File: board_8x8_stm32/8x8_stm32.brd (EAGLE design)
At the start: 100 x 100 mm, 96 parts, among them IC1 STM32F0, J1 SWD_SHROUD, Q1 BSS123, Q10 BSS84, Q11 BSS84, Q12 BSS84, Q13 BSS84, Q14 BSS84, Q15 BSS84, Q16 BSS84, Q2 BSS123, Q3 BSS123, Q4 BSS123, Q5 BSS123, Q6 BSS123, Q7 BSS123, Q8 BSS123, Q9 BSS84

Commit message: adding led photodide sim
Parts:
- removed D1, D2, D3, D4, D5, D6, D7, D8: (no value), dtb:SOD123
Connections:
- removed net CHARGE: D1.C, D2.C, D3.C, D4.C, D5.C, D6.C, D7.C, D8.C
- net ROW1: no longer D1.A
- net ROW2: no longer D2.A
- net ROW3: no longer D3.A
- net ROW4: no longer D4.A
- net ROW5: no longer D5.A
- net ROW6: no longer D6.A
- net ROW7: no longer D7.A
- net ROW8: no longer D8.A
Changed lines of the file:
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@@
 <element name="Q15" library="transistor-small-signal" package="SOT23" value="BSS84" x="67.29" y="41.4" rot="R270"/>
 <element name="Q16" library="transistor-small-signal" package="SOT23" value="BSS84" x="79.29" y="59.02" rot="R270"/>
-<element name="D1" library="dtb" package="SOD123" value="" x="-16.51" y="69.85"/>
-<element name="D2" library="dtb" package="SOD123" value="" x="-22.86" y="69.85"/>
-<element name="D3" library="dtb" package="SOD123" value="" x="-29.21" y="69.85"/>
-<element name="D4" library="dtb" package="SOD123" value="" x="-35.56" y="69.85"/>
-<element name="D5" library="dtb" package="SOD123" value="" x="-41.91" y="69.85"/>
-<element name="D6" library="dtb" package="SOD123" value="" x="-48.26" y="69.85"/>
-<element name="D7" library="dtb" package="SOD123" value="" x="-54.61" y="69.85"/>
-<element name="D8" library="dtb" package="SOD123" value="" x="-60.96" y="69.85"/>
 <element name="J1" library="dtb" package="SWD_PTH_SHROUD" value="SWD_SHROUD" x="75" y="49.9" rot="MR270"/>
 <element name="SV1" library="con-lstb" package="MA03-2" value="" x="50.27" y="74.08">
@@
 <contactref element="LED8" pad="A"/>
 <contactref element="Q9" pad="3"/>
-<contactref element="D1" pad="A"/>
-<wire x1="-14.61" y1="69.85" x2="36.44" y2="73.77" width="0" layer="19" extent="1-1"/>
-<wire x1="-44.45" y1="61.48" x2="-14.61" y2="69.85" width="0" layer="19" extent="1-1"/>
+<wire x1="-44.45" y1="61.48" x2="36.44" y2="73.77" width="0" layer="19" extent="1-1"/>
 </signal>
 <signal name="ROW2">
@@
 <contactref element="LED15" pad="A"/>
 <contactref element="Q10" pad="3"/>
-<contactref element="D2" pad="A"/>
-<wire x1="-20.96" y1="69.85" x2="26.82" y2="73.77" width="0" layer="19" extent="1-1"/>
-<wire x1="-52.07" y1="31" x2="-20.96" y2="69.85" width="0" layer="19" extent="1-1"/>
+<wire x1="-52.07" y1="31" x2="26.82" y2="73.77" width="0" layer="19" extent="1-1"/>
 <wire x1="-55.88" y1="31" x2="-52.07" y2="31" width="0" layer="19" extent="1-1"/>
 </signal>
@@
 <contactref element="LED24" pad="A"/>
 <contactref element="Q11" pad="3"/>
-<contactref element="D3" pad="A"/>
 <wire x1="67.77" y1="65.8" x2="93.75" y2="68" width="0" layer="19" extent="1-1"/>
-<wire x1="-27.31" y1="69.85" x2="67.77" y2="65.8" width="0" layer="19" extent="1-1"/>
 </signal>
 <signal name="ROW4">
 <contactref element="LED32" pad="A"/>
 <contactref element="Q16" pad="3"/>
-<contactref element="D4" pad="A"/>
 <wire x1="80.39" y1="59.02" x2="93.75" y2="55.5" width="0" layer="19" extent="1-1"/>
-<wire x1="-33.66" y1="69.85" x2="80.39" y2="59.02" width="0" layer="19" extent="1-1"/>
 </signal>
 <signal name="ROW5">
 <contactref element="LED40" pad="A"/>
 <contactref element="Q15" pad="3"/>
-<contactref element="D5" pad="A"/>
 <wire x1="68.39" y1="41.4" x2="93.75" y2="43" width="0" layer="19" extent="1-1"/>
-<wire x1="-40.01" y1="69.85" x2="68.39" y2="41.4" width="0" layer="19" extent="1-1"/>
 </signal>
 <signal name="ROW6">
 <contactref element="LED48" pad="A"/>
 <contactref element="Q14" pad="3"/>
-<contactref element="D6" pad="A"/>
 <wire x1="80.39" y1="28.78" x2="93.75" y2="30.5" width="0" layer="19" extent="1-1"/>
-<wire x1="-46.36" y1="69.85" x2="80.39" y2="28.78" width="0" layer="19" extent="1-1"/>
 </signal>
 <signal name="ROW7">
@@
 <contactref element="LED55" pad="A"/>
 <contactref element="Q13" pad="3"/>
-<contactref element="D7" pad="A"/>
 <wire x1="81.25" y1="18" x2="93.75" y2="18" width="0" layer="19" extent="1-1"/>
 <wire x1="68.75" y1="18" x2="81.25" y2="18" width="0" layer="19" extent="1-1"/>
@@
 <wire x1="18.75" y1="18" x2="31.25" y2="18" width="0" layer="19" extent="1-1"/>
 <wire x1="6.25" y1="18" x2="18.75" y2="18" width="0" layer="19" extent="1-1"/>
-<wire x1="-52.71" y1="69.85" x2="6.25" y2="18" width="0" layer="19" extent="1-1"/>
 </signal>
 <signal name="ROW8">
@@
 <contactref element="LED57" pad="A"/>
 <contactref element="Q12" pad="3"/>
-<contactref element="D8" pad="A"/>
 <wire x1="81.25" y1="5.5" x2="93.75" y2="5.5" width="0" layer="19" extent="1-1"/>
 <wire x1="68.75" y1="5.5" x2="81.25" y2="5.5" width="0" layer="19" extent="1-1"/>
@@
 <wire x1="18.75" y1="5.5" x2="31.25" y2="5.5" width="0" layer="19" extent="1-1"/>
 <wire x1="6.25" y1="5.5" x2="18.75" y2="5.5" width="0" layer="19" extent="1-1"/>
-<wire x1="-59.06" y1="69.85" x2="6.25" y2="5.5" width="0" layer="19" extent="1-1"/>
 </signal>
 <signal name="COL8">
@@
 <wire x1="29" y1="32.9" x2="40.48" y2="32.045" width="0" layer="19" extent="1-1"/>
 </signal>
-<signal name="CHARGE">
-<contactref element="D1" pad="C"/>
-<contactref element="D8" pad="C"/>
-<contactref element="D7" pad="C"/>
-<contactref element="D6" pad="C"/>
-<contactref element="D5" pad="C"/>
-<contactref element="D4" pad="C"/>
-<contactref element="D3" pad="C"/>
-<contactref element="D2" pad="C"/>
-<wire x1="-24.76" y1="69.85" x2="-18.41" y2="69.85" width="0" layer="19" extent="1-1"/>
-<wire x1="-31.11" y1="69.85" x2="-24.76" y2="69.85" width="0" layer="19" extent="1-1"/>
-<wire x1="-37.46" y1="69.85" x2="-31.11" y2="69.85" width="0" layer="19" extent="1-1"/>
-<wire x1="-43.81" y1="69.85" x2="-37.46" y2="69.85" width="0" layer="19" extent="1-1"/>
-<wire x1="-50.16" y1="69.85" x2="-43.81" y2="69.85" width="0" layer="19" extent="1-1"/>
-<wire x1="-56.51" y1="69.85" x2="-50.16" y2="69.85" width="0" layer="19" extent="1-1"/>
-<wire x1="-62.86" y1="69.85" x2="-56.51" y2="69.85" width="0" layer="19" extent="1-1"/>
-</signal>
 <signal name="RFET1">

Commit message: playing about with different deisgns
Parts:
- moved Q13 46.4 mm to (79.5, 16.4), turned to 0 degrees
- moved Q12 46.2 mm to (79.3, 3.92), turned to 0 degrees
- moved Q8 13.9 mm to (72.8, 31.0), turned to 180 degrees
- moved Q11 12.8 mm to (79.5, 66.2), turned to 0 degrees
- moved Q15 12.3 mm to (79.6, 41.0), turned to 0 degrees
- moved Q5 11.9 mm to (65.5, 31.0)
- moved J1 11.5 mm to (86.5, 49.6)
- moved Q16 5.25 mm to (79.7, 53.8), turned to 0 degrees
- moved RN2 4.46 mm to (69.2, 27.5), turned to 0 degrees
- moved Q6 3.25 mm to (59.2, 31.0)
- moved Q7 1.82 mm to (53.5, 30.8), turned to 180 degrees
- moved Q14 0.50 mm to (79.7, 29.0), turned to 0 degrees
- moved LED36 0.50 mm to (43.8, 43.8)
- moved IC1 0.26 mm to (50.0, 49.9), turned to 180 degrees
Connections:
- removed net SHIFT_CLK: SV2.2, SV4.2
- new net N$9: Q10.2, Q11.2, Q12.2, Q13.2, Q14.2, Q15.2, Q16.2, Q9.2
- new net SHIFT_LEFT: SV4.5
- new net SHIFT_RIGHT: SV2.5
- net CFET1: now also IC1.18
- net CFET2: now also IC1.19
- net CFET3: now also IC1.20
- net CFET4: now also IC1.39
- net CFET5: now also IC1.40
- net CFET6: now also IC1.41
- net CFET7: now also IC1.42
- net CFET8: now also IC1.43
- net COL1: now also IC1.45
- net COL2: now also IC1.46
- net COL3: now also IC1.21
- net COL4: now also IC1.22
- net COL5: now also IC1.25
- net COL6: now also IC1.26
- net COL7: now also IC1.27
- net COL8: now also IC1.28
- net ROW1: now also LED1.A, LED2.A, LED3.A, LED4.A, LED5.A, LED6.A, LED7.A
- net ROW2: now also LED10.A, LED11.A, LED12.A, LED13.A, LED14.A, LED9.A
- net ROW3: now also LED17.A, LED18.A, LED19.A, LED20.A, LED21.A, LED22.A, LED23.A
- net ROW4: now also LED25.A, LED26.A, LED27.A, LED28.A, LED29.A, LED30.A, LED31.A
- net ROW5: now also LED33.A, LED34.A, LED35.A, LED36.A, LED37.A, LED38.A, LED39.A
- net ROW6: now also LED41.A, LED42.A, LED43.A, LED44.A, LED45.A, LED46.A, LED47.A
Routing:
- net COL8: track 0.00 -> 149.2 mm, vias 0 -> 9
- net COL1: track 0.00 -> 132.3 mm, vias 0 -> 7
- net COL2: track 0.00 -> 118.4 mm, vias 0 -> 7
- net ROW5: track 0.00 -> 92.6 mm, vias 0 -> 5
- net ROW3: track 0.00 -> 88.2 mm
- net COL3: track 0.00 -> 88.0 mm, vias 0 -> 6
- net ROW4: track 0.00 -> 83.2 mm
- net COL7: track 0.00 -> 76.5 mm, vias 0 -> 7
- net SWDAT: track 0.00 -> 41.9 mm, vias 0 -> 4
- net COL6: track 0.00 -> 41.5 mm, vias 0 -> 4
- net GND: track 0.00 -> 39.4 mm, vias 0 -> 4
- net COL5: track 0.00 -> 36.0 mm, vias 0 -> 4
- net SWCLK: track 0.00 -> 35.0 mm, vias 0 -> 2
- net CFET8: track 0.00 -> 33.6 mm
- net CFET7: track 0.00 -> 28.8 mm, vias 0 -> 2
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
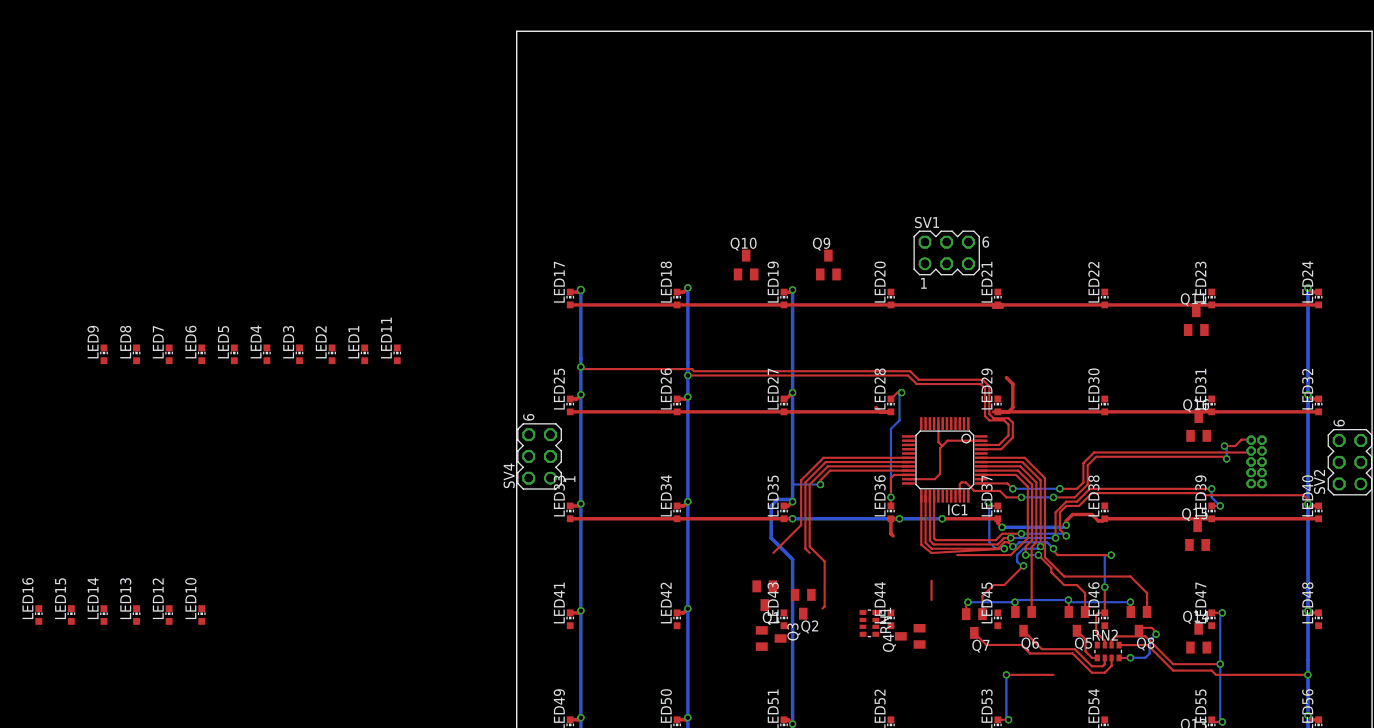
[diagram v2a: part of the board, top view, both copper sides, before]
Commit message: postioning components to the top edge
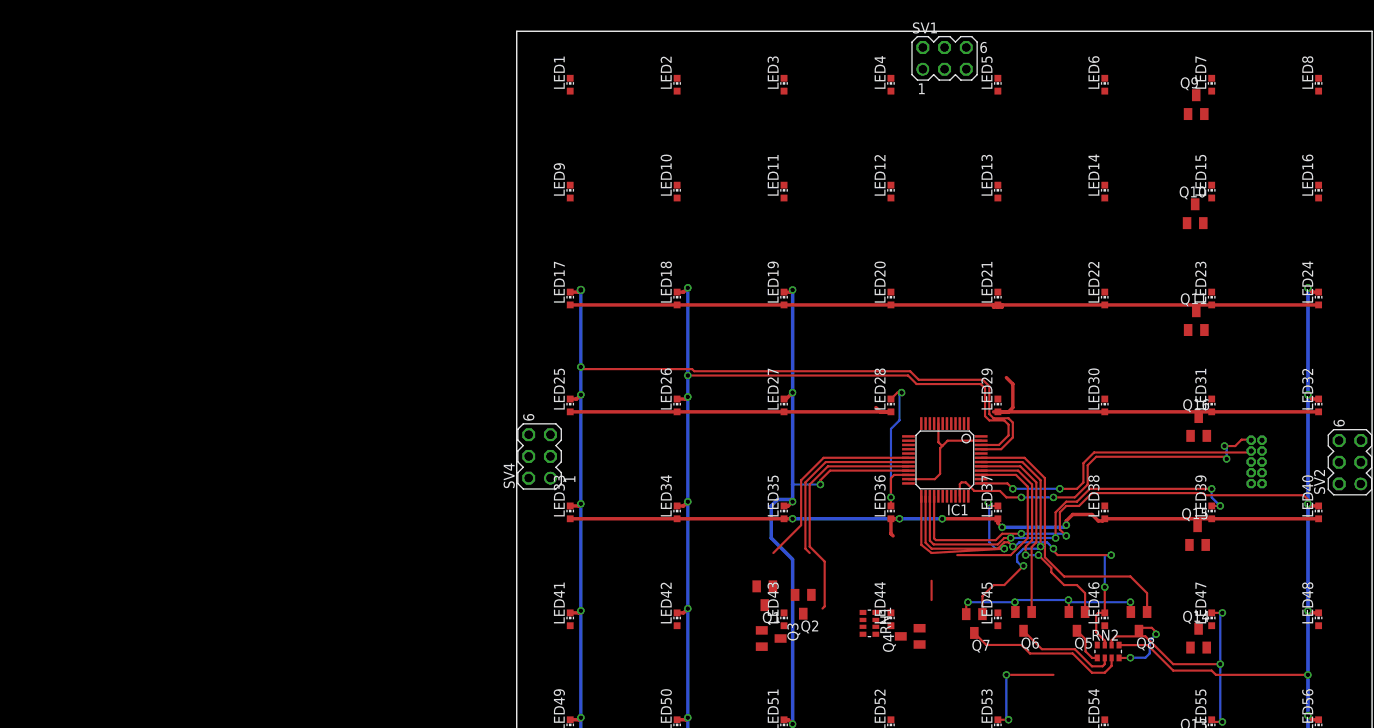
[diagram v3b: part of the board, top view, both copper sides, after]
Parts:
- moved LED16 157.6 mm to (93.8, 81.2)
- moved LED15 142.2 mm to (81.2, 81.2)
- moved LED8 141.7 mm to (93.8, 93.8)
- moved LED14 127.0 mm to (68.8, 81.2)
- moved LED7 125.9 mm to (81.2, 93.8)
- moved LED13 112.2 mm to (56.2, 81.2)
- moved LED6 110.2 mm to (68.8, 93.8)
- moved LED12 97.8 mm to (43.8, 81.2)
- moved LED5 94.7 mm to (56.2, 93.8)
- moved LED4 79.5 mm to (43.8, 93.8)
- moved LED10 74.4 mm to (18.8, 81.2)
- moved LED3 64.8 mm to (31.2, 93.8)
- moved LED9 57.7 mm to (6.25, 81.2)
- moved Q10 52.8 mm to (79.3, 78.7)
- moved LED2 51.2 mm to (18.8, 93.8)
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
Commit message: adding a couple of notes
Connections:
- removed net N$9: Q10.2, Q11.2, Q12.2, Q13.2, Q14.2, Q15.2, Q16.2, Q9.2
- new net +5V: Q10.2, Q11.2, Q12.2, Q13.2, Q14.2, Q15.2, Q16.2, Q9.2, SV2.6, SV4.6
- new net N$10: IC1.30
- net +3V3: now also SV2.2, SV4.2
- net G_UART: now also IC1.31
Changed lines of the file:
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@@
 <contactref element="SV3" pad="4"/>
 <contactref element="SV2" pad="4"/>
-<wire x1="96.15" y1="49.61" x2="50.02" y2="98.1" width="0" layer="19" extent="1-1"/>
-<wire x1="49.2" y1="4.35" x2="96.15" y2="49.61" width="0" layer="19" extent="1-1"/>
-<wire x1="1.4" y1="50.29" x2="49.2" y2="4.35" width="0" layer="19" extent="1-1"/>
+<contactref element="IC1" pad="31"/>
+<wire x1="50.3" y1="45.63" x2="50.02" y2="98.1" width="0" layer="19" extent="1-1"/>
+<wire x1="49.2" y1="4.35" x2="50.3" y2="45.63" width="0" layer="19" extent="1-1"/>
+<wire x1="96.15" y1="49.61" x2="50.3" y2="45.63" width="0" layer="19" extent="1-1"/>
+<wire x1="1.4" y1="50.29" x2="50.3" y2="45.63" width="0" layer="19" extent="1-1"/>
 </signal>
 <signal name="NRST">
@@
 <contactref element="IC1" pad="1"/>
 <contactref element="J1" pad="1"/>
+<contactref element="SV4" pad="2"/>
+<contactref element="SV2" pad="2"/>
+<wire x1="87.135" y1="52.19" x2="96.15" y2="47.07" width="0" layer="19" extent="1-1"/>
 <wire x1="54.3" y1="52.63" x2="87.135" y2="52.19" width="0" layer="19" extent="1-1"/>
 <wire x1="52.8" y1="54.13" x2="54.3" y2="52.63" width="0" layer="19" extent="1-1"/>
 <wire x1="48.8" y1="54.13" x2="52.8" y2="54.13" width="0" layer="19" extent="1-1"/>
 <wire x1="45.8" y1="47.13" x2="48.8" y2="54.13" width="0" layer="19" extent="1-1"/>
+<wire x1="1.4" y1="47.75" x2="45.8" y2="47.13" width="0" layer="19" extent="1-1"/>
 </signal>
 <signal name="SHIFT_LEFT">
@@
 <contactref element="SV2" pad="5"/>
 </signal>
-<signal name="N$9">
+<signal name="N$10">
+<contactref element="IC1" pad="30"/>
+</signal>
+<signal name="+5V">
 <contactref element="Q12" pad="2"/>
 <contactref element="Q9" pad="2"/>
@@
 <contactref element="Q14" pad="2"/>
 <contactref element="Q13" pad="2"/>
+<contactref element="SV4" pad="6"/>
+<contactref element="SV2" pad="6"/>
 <wire x1="80.27" y1="77.57" x2="80.39" y2="90.32" width="0" layer="19" extent="1-1"/>
 <wire x1="80.4" y1="65.07" x2="80.27" y2="77.57" width="0" layer="19" extent="1-1"/>
@@
 <wire x1="80.41" y1="15.32" x2="80.67" y2="27.94" width="0" layer="19" extent="1-1"/>
 <wire x1="80.28" y1="2.82" x2="80.41" y2="15.32" width="0" layer="19" extent="1-1"/>
+<wire x1="96.15" y1="52.15" x2="80.68" y2="52.69" width="0" layer="19" extent="1-1"/>
+<wire x1="1.4" y1="52.83" x2="80.68" y2="52.69" width="0" layer="19" extent="1-1"/>
 </signal>
 </signals>

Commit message: 'done' schematic
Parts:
- added C1, C2, C3, C4, C5, C6, C7, C8: 100p, passives-7351:C0603-N
- added C10, C11, C16, C9: (no value), passives-7351:C0603-N
- added C12, C13: (no value), rcl:E2-4
- added C14, C15: (no value), rcl:C050-025X075
- added JP1: (no value), Mine:1X02
- added JP2: (no value), SparkFun-Connectors:1X06
- added JP3, JP4, JP5, JP6: (no value), SparkFun-Connectors:1X08_ROUND
- added LED65: (no value), dtb:LED5MM
- added LED66: (no value), dtb:LED10MM
- added R1, R2, R3, R4, R5, R6, R7, R8: DNP, passives-7351:R0603-N
- added R10: 2k2, passives-7351:R0603-N
- added R9: (no value), passives-7351:R0603-N
- added RN3, RN4: (no value), resistor-dil:EXB38V
- added SJ1, SJ2: (no value), SparkFun-Passives:PAD-JUMPER-2-NC_BY_TRACE_YES_SILK
- added U$1: MCP1700, dtb:TO92-INLINE
- moved RN2 50.5 mm to (39.6, 68.5)
- moved Q1 42.8 mm to (60.0, 63.5), turned to 0 degrees
- moved Q8 42.1 mm to (46.0, 63.5), turned to 0 degrees
- moved Q5 41.9 mm to (39.0, 63.5), turned to 0 degrees
- moved Q3 41.6 mm to (53.0, 63.5), turned to 0 degrees
- moved RN1 38.8 mm to (51.2, 68.2), turned to 0 degrees
- moved Q2 38.2 mm to (56.5, 63.5), turned to 0 degrees
- moved Q7 37.4 mm to (35.5, 63.5), turned to 0 degrees
- moved Q6 36.6 mm to (42.5, 63.5), turned to 0 degrees
- moved Q4 34.4 mm to (49.5, 63.5), turned to 0 degrees
- moved Q14 0.22 mm to (79.5, 29.0)
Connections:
- removed net N$10: IC1.30
- new net N$11: IC1.4, R10.2
- new net N$9: IC1.44, JP1.2, R9.1
- net +3V3: now also C10.1, C11.1, C15.1, C16.1, C9.1, JP2.4, JP3.5, JP4.5, JP5.5, JP6.5, R9.2, U$1.VOUT
- net +5V: now also C12.+, C13.+, C14.1, JP3.1, JP3.8, JP4.1, JP4.8, JP5.1, JP5.8, JP6.1, JP6.8, RN3.1, RN3.2, RN3.3, RN3.4, RN4.1, RN4.2, RN4.3, RN4.4, U$1.VIN
- net CFET1: now also IC1.10; no longer IC1.18
- net CFET2: now also IC1.11; no longer IC1.19
- net CFET3: now also IC1.12; no longer IC1.20
- net CFET4: now also IC1.13; no longer IC1.39
- net CFET5: now also IC1.14; no longer IC1.40
- net CFET6: now also IC1.15; no longer IC1.41
- net CFET7: now also IC1.16; no longer IC1.42
- net CFET8: now also IC1.17; no longer IC1.43
- net COL1: now also C1.1, R1.2, RN1.5; no longer RN1.8
- net COL2: now also C2.1, R2.2, RN1.6; no longer RN1.7
- net COL3: now also C3.1, R3.2, RN1.7; no longer RN1.6
- net COL4: now also C4.1, R4.2, RN1.8; no longer RN1.5
- net COL5: now also C5.1, R5.2
- net COL6: now also C6.1, R6.2
- net COL7: now also C7.1, R7.2
- net COL8: now also C8.1, R10.1, R8.2; no longer IC1.28
- net COMMS_DOWN: now also IC1.19, JP5.3
- net COMMS_LEFT: now also IC1.3, JP4.3
- net COMMS_RIGHT: now also IC1.2, JP3.3
- net COMMS_UP: now also IC1.18, JP6.3
- net GND: now also C1.2, C10.2, C11.2, C12.-, C13.-, C14.2, C15.2, C16.2, C2.2, C3.2, C4.2, C5.2, C6.2, C7.2, C8.2, C9.2, JP1.1, JP2.6, JP3.2, JP3.7, JP4.2, JP4.7, JP5.2, JP5.7, JP6.2, JP6.7, R1.1, R2.1, R3.1, R4.1, R5.1, R6.1, R7.1, R8.1, U$1.GND
- net G_UART: now also JP2.3, JP3.6, JP4.6, JP5.6, JP6.6
- net N$5: now also RN1.1; no longer RN1.4
- net N$6: now also RN1.2; no longer RN1.3
- net N$7: now also RN1.3; no longer RN1.2
- net N$8: now also RN1.4; no longer RN1.1
- net RFET1: now also IC1.29, RN4.7
- net RFET2: now also IC1.30, JP2.2, RN4.6
- net RFET3: now also IC1.28, RN4.8
- net RFET4: now also IC1.32, RN4.5
- net RFET5: now also IC1.33, RN3.5
- net RFET6: now also RN3.6, SJ1.2
- net RFET7: now also RN3.7, SJ2.2
- net RFET8: now also IC1.38, RN3.8
- net ROW1: now also IC1.5
- net ROW2: now also IC1.6
- net ROW3: now also IC1.20
- net ROW4: now also IC1.39
- net ROW5: now also IC1.40
- net ROW6: now also IC1.41
- net ROW7: now also IC1.42
- net ROW8: now also IC1.43
- net SHIFT_LEFT: now also IC1.36, JP4.4
- net SHIFT_RIGHT: now also IC1.35, JP3.4
- net SWCLK: now also SJ2.1
- net SWDAT: now also SJ1.1
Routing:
- net +5V: track 0.00 -> 432.6 mm
- net G_UART: track 0.00 -> 185.5 mm, vias 0 -> 12
- net COL8: track 149.2 -> 3.69 mm, vias 9 -> 0
- net COL1: track 132.3 -> 6.79 mm, vias 7 -> 0
- net ROW5: track 92.6 -> 0.00 mm, vias 5 -> 0
- net COMMS_DOWN: track 0.00 -> 82.5 mm, vias 0 -> 8
- net SHIFT_LEFT: track 0.00 -> 73.0 mm, vias 0 -> 4
- net ROW6: track 0.00 -> 72.1 mm
- net ROW7: track 0.00 -> 69.6 mm
- net COL7: track 76.5 -> 7.52 mm, vias 7 -> 0
- net ROW4: track 83.2 -> 19.2 mm
- net RFET1: track 0.00 -> 63.7 mm
- net ROW3: track 88.2 -> 27.8 mm
- net COMMS_LEFT: track 0.00 -> 54.1 mm
- net RFET2: track 0.00 -> 50.2 mm
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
